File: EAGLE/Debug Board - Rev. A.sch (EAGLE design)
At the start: 5 parts, among them J1 M50-3032042, J2 M50-3032042, J3 224920, J4 M50-3031042, J5 DF12NB-40DS-0.5V_51_

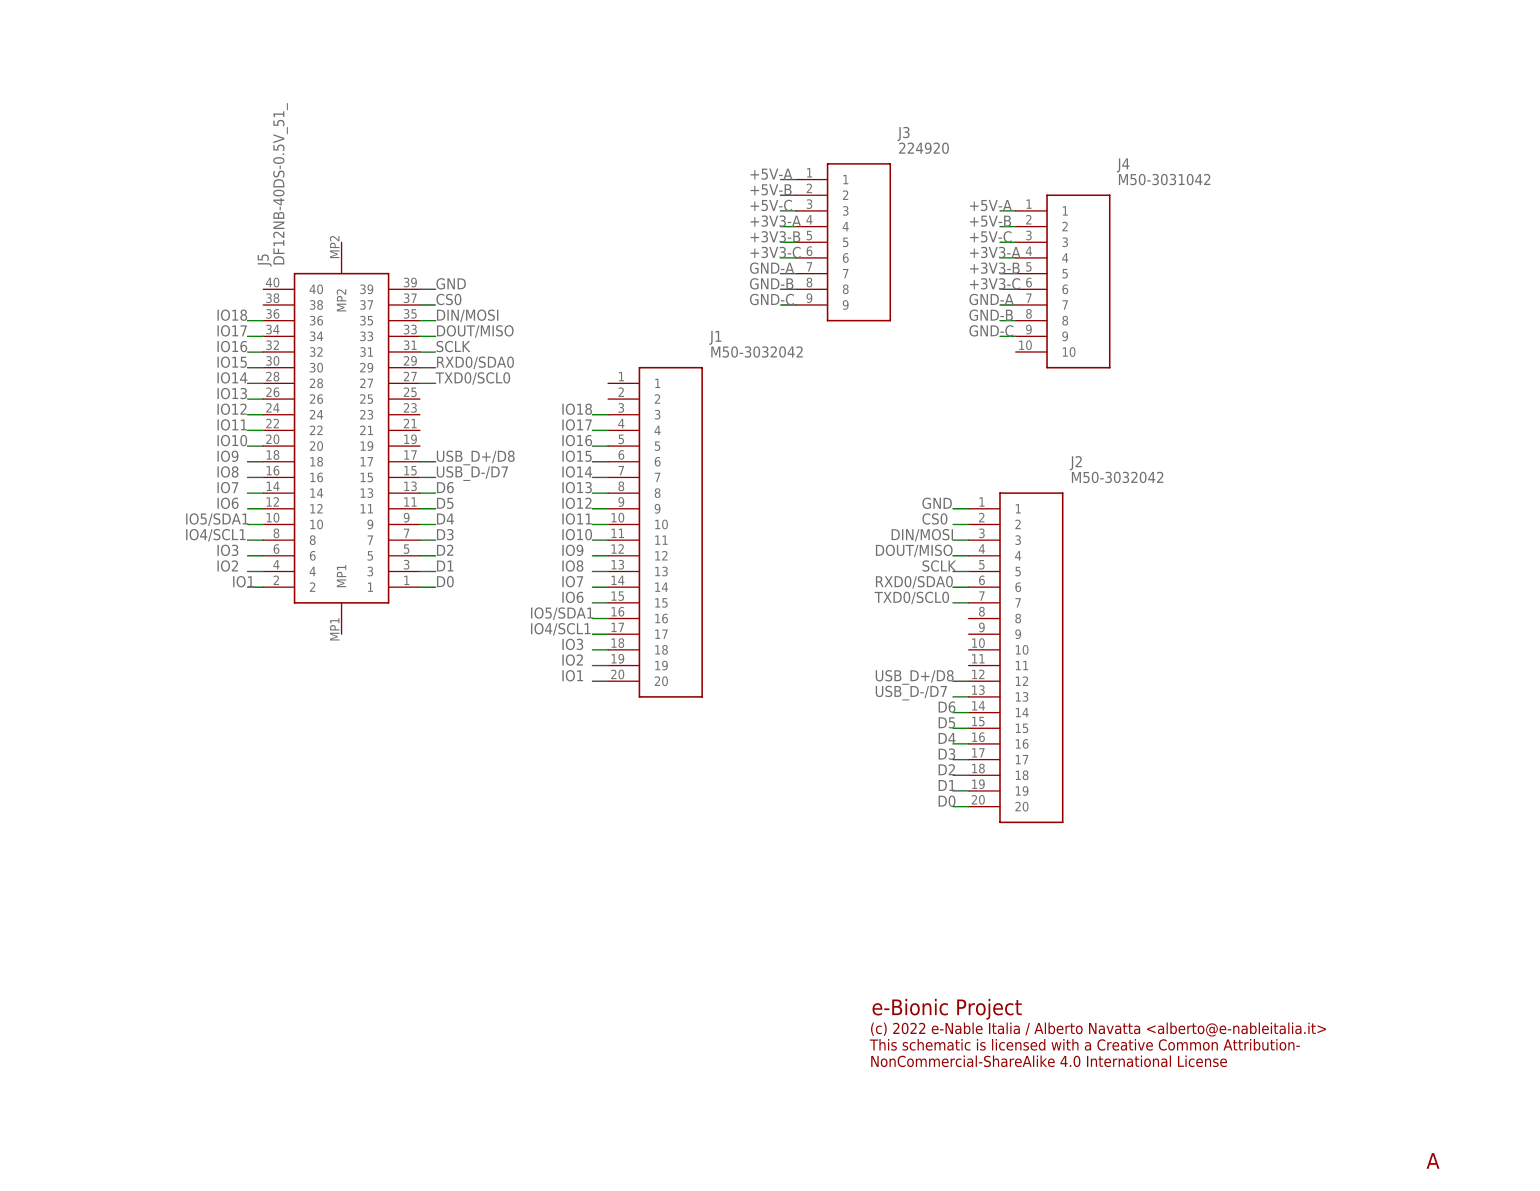
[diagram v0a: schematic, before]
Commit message: Updated Debug Board to Rev. A:
Added power and data bus connector on the bottom side of the board
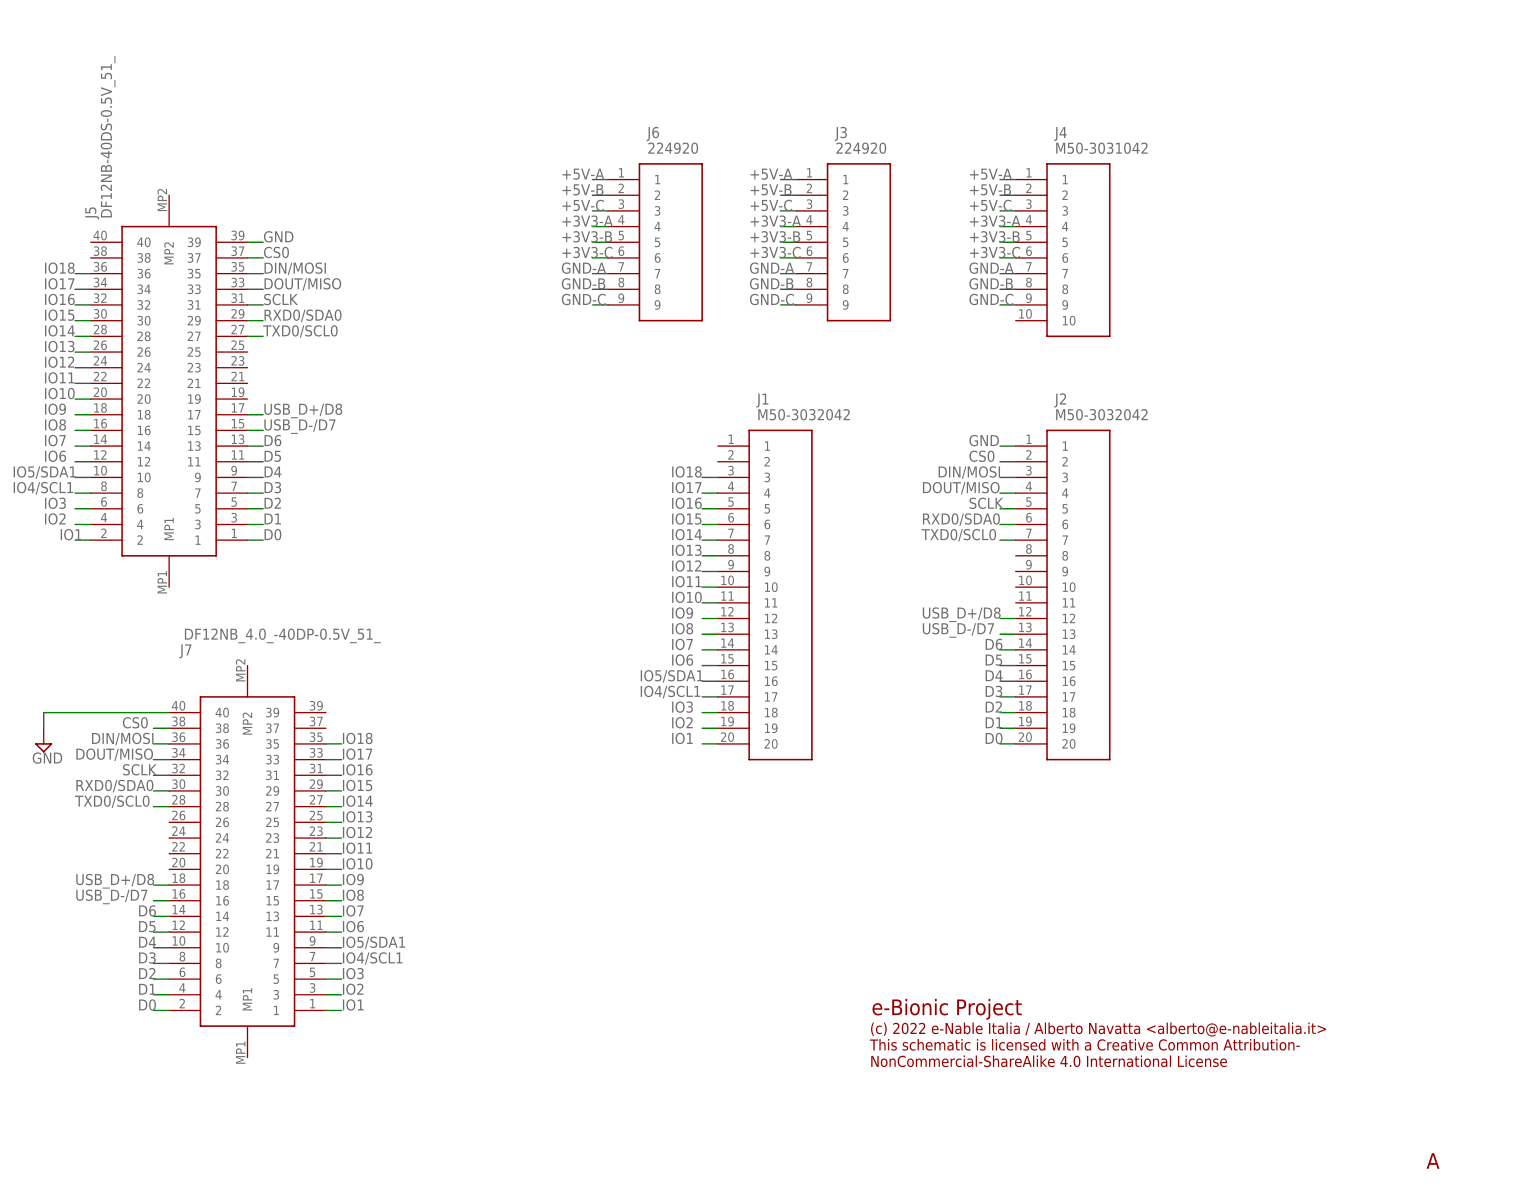
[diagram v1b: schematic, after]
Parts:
- added J6: 224920, SamacSys_Parts:224920
- added J7: DF12NB_4.0_-40DP-0.5V_51_, SamacSys_Parts:DF12NB_4.0_-40DP-0.5V_51_
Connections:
- net +3V3-A: now also J6.4
- net +3V3-B: now also J6.5
- net +3V3-C: now also J6.6
- net +5V-A: now also J6.1
- net +5V-B: now also J6.2
- net +5V-C: now also J6.3
- net CS0: now also J7.38
- net D0: now also J7.2
- net D1: now also J7.4
- net D2: now also J7.6
- net D3: now also J7.8
- net D4: now also J7.10
- net D5: now also J7.12
- net D6: now also J7.14
- net DIN/MOSI: now also J7.36
- net DOUT/MISO: now also J7.34
- net GND: now also J7.40
- net GND-A: now also J6.7
- net GND-B: now also J6.8
- net GND-C: now also J6.9
- net IO1: now also J7.1
- net IO10: now also J7.19
- net IO11: now also J7.21
- net IO12: now also J7.23
- net IO13: now also J7.25
- net IO14: now also J7.27
- net IO15: now also J7.29
- net IO16: now also J7.31
- net IO17: now also J7.33
- net IO18: now also J7.35
- net IO2: now also J7.3
- net IO3: now also J7.5
- net IO4/SCL1: now also J7.7
- net IO5/SDA1: now also J7.9
- net IO6: now also J7.11
- net IO7: now also J7.13
- net IO8: now also J7.15
- net IO9: now also J7.17
- net RXD0/SDA0: now also J7.30
- net SCLK: now also J7.32
- net TXD0/SCL0: now also J7.28
- net USB_D+/D8: now also J7.18
- net USB_D-/D7: now also J7.16
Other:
- moved on the sheet: J1, J2, J4, J5
